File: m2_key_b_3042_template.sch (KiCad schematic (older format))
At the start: 1 part, among them J1 M.2_Key_B

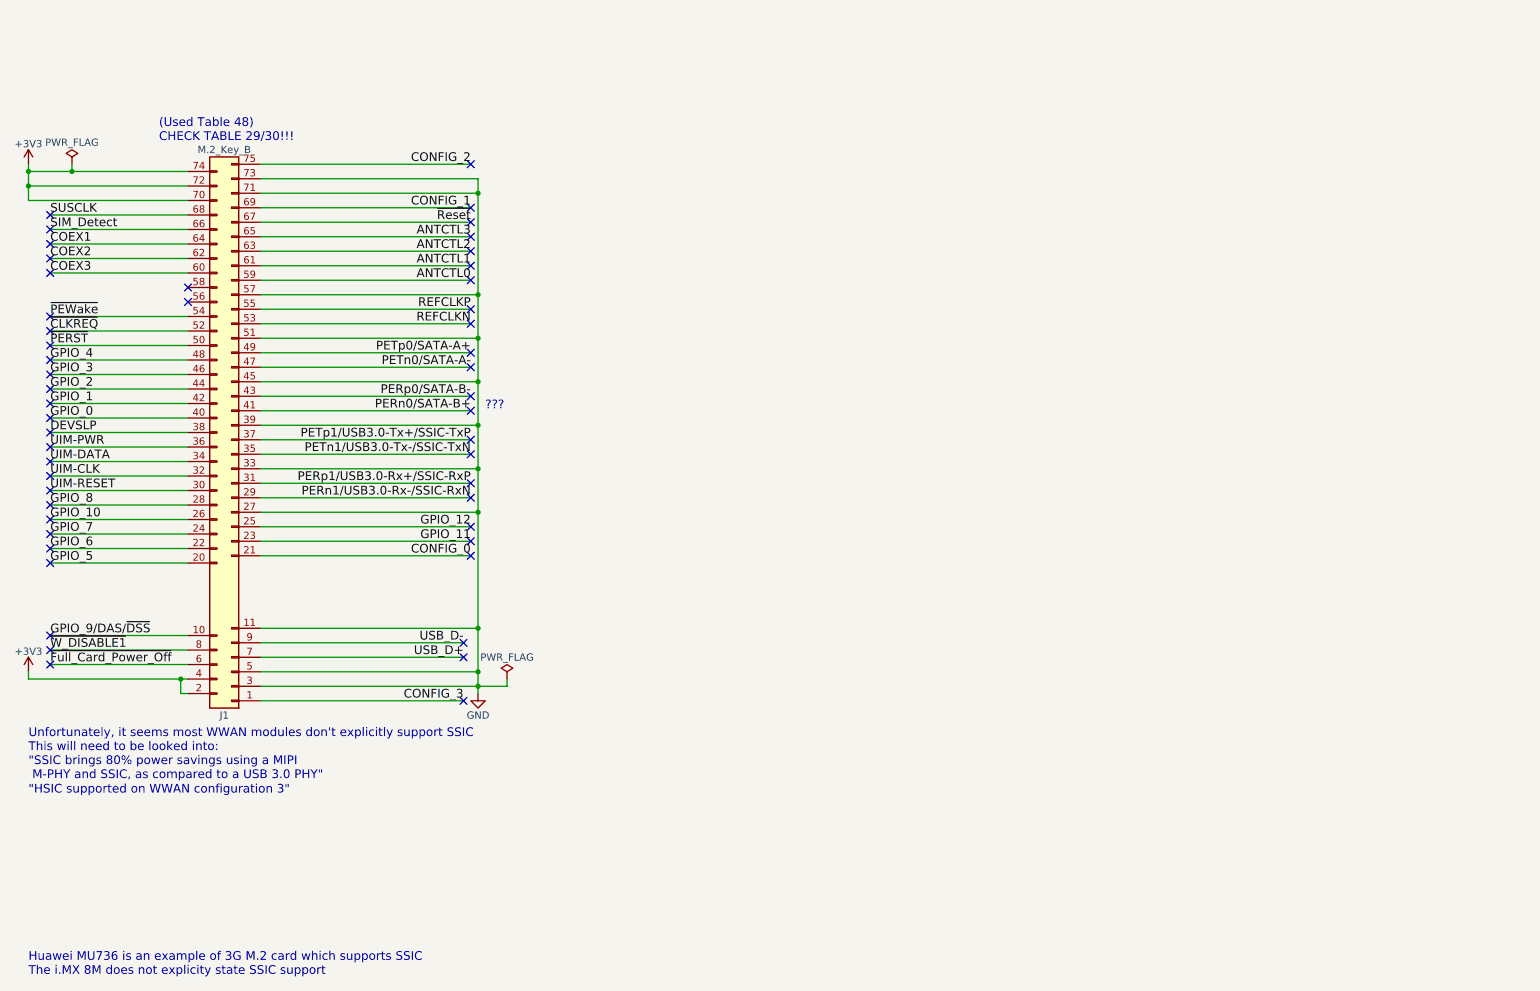
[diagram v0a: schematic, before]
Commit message: Include MHF4 coax connectors for the baseband, diversity, and GNSS antennae
Improved the soldermask and mounting hole.
Included silkscreen designating the component area.
Antennae MHF4 coax connectors show what orientation they need to be placed in (chamfer).
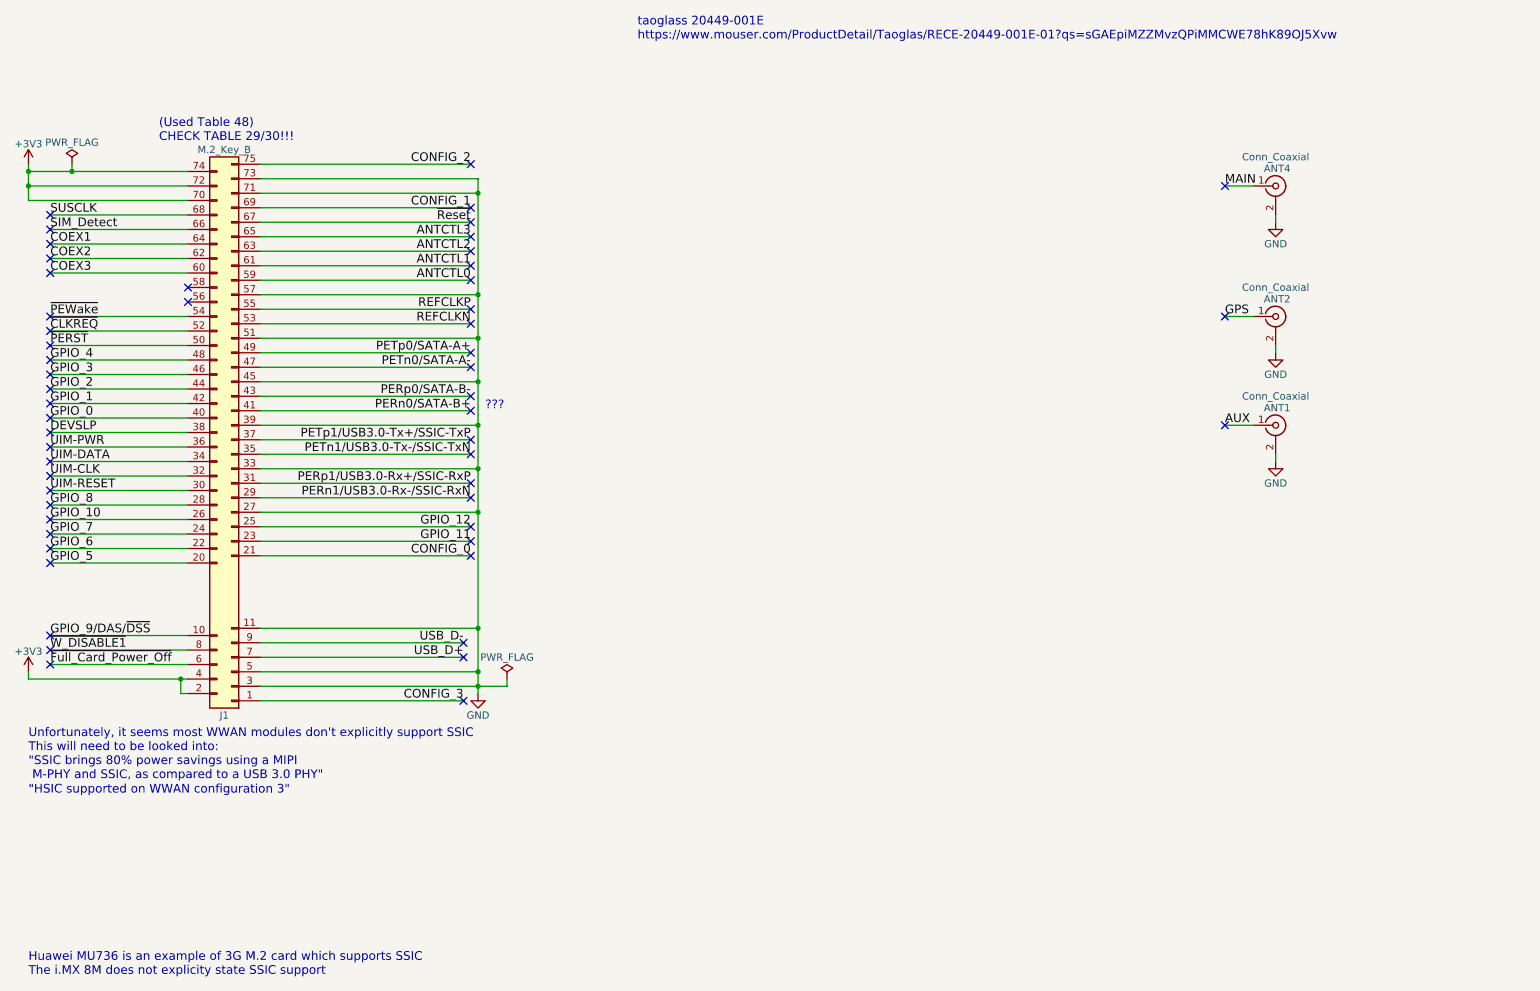
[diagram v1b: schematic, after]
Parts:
- added ANT1, ANT2, ANT4: Conn_Coaxial, m2_key_b_3042:MHF4_20449-001E, symbol Conn_Coaxial
- J1: footprint m2_key_b:m2_key_b_gold_fingers -> m2_key_b_3042:M.2_Key_B_Gold_Fingers
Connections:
- net GND: now also ANT1.2 (Ext), ANT2.2 (Ext), ANT4.2 (Ext)
- new net AUX: ANT1.1 (In)
- new net GPS: ANT2.1 (In)
- new net MAIN: ANT4.1 (In)
- no-connect marks 51 -> 54
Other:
- note added: "taoglass 20449-001E\nhttps://www.mouser.com/ProductDetail/Taoglas/RECE-20449-001E-01?qs=sGAEpiMZZMvzQPiMMCWE78hK89OJ5Xvw"
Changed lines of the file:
@@
 LIBS:contrib
 LIBS:valves
-LIBS:m2_key_b_template
-LIBS:m2_key_b_template-cache
+LIBS:m2_key_b_3042_template
+LIBS:m2_key_b_3042_template-cache
 EELAYER 25 0
 EELAYER END
@@
 F 0 "J1" H 3000 5600 50  0000 C CNN
 F 1 "M.2_Key_B" H 3000 1700 50  0000 C CNN
-F 2 "m2_key_b:m2_key_b_gold_fingers" H 2950 3700 50  0001 C CNN
+F 2 "m2_key_b_3042:M.2_Key_B_Gold_Fingers" H 2950 3700 50  0001 C CNN
 F 3 "" H 2950 3700 50  0001 C CNN
 	1    2950 3700
@@
 $EndComp
 Wire Wire Line
-	2650 1850 1550 1850
+	1550 1850 2650 1850
 Wire Wire Line
 	1550 1800 1550 2050
@@
 Wire Wire Line
 	4850 5400 4850 5350
+Text Notes 5750 950  0    60   ~ 0
+taoglass 20449-001E\nhttps://www.mouser.com/ProductDetail/Taoglas/RECE-20449-001E-01?qs=sGAEpiMZZMvzQPiMMCWE78hK89OJ5Xvw
+$Comp
+L Conn_Coaxial ANT1
+U 1 1 5AA9D3C4
+P 10150 3600
+F 0 "ANT1" H 10160 3720 50  0000 C CNN
+F 1 "Conn_Coaxial" H 10150 3800 50  0000 C CNN
+F 2 "m2_key_b_3042:MHF4_20449-001E" H 10150 3600 50  0001 C CNN
+F 3 "" H 10150 3600 50  0001 C CNN
+	1    10150 3600
+	1    0    0    -1
+$EndComp
+$Comp
+L Conn_Coaxial ANT2
+U 1 1 5AA9D4DD
+P 10150 2850
+F 0 "ANT2" H 10160 2970 50  0000 C CNN
+F 1 "Conn_Coaxial" H 10150 3050 50  0000 C CNN
+F 2 "m2_key_b_3042:MHF4_20449-001E" H 10150 2850 50  0001 C CNN
+F 3 "" H 10150 2850 50  0001 C CNN
+	1    10150 2850
+	1    0    0    -1
+$EndComp
+$Comp
+L Conn_Coaxial ANT4
+U 1 1 5AA9D54E
+P 10150 1950
+F 0 "ANT4" H 10160 2070 50  0000 C CNN
+F 1 "Conn_Coaxial" H 10150 2150 50  0000 C CNN
+F 2 "m2_key_b_3042:MHF4_20449-001E" H 10150 1950 50  0001 C CNN
+F 3 "" H 10150 1950 50  0001 C CNN
+	1    10150 1950
+	1    0    0    -1
+$EndComp
+$Comp
+L GND #PWR06
+U 1 1 5AA9D64F
+P 10150 2200
+F 0 "#PWR06" H 10150 1950 50  0001 C CNN
+F 1 "GND" H 10150 2050 50  0000 C CNN
+F 2 "" H 10150 2200 50  0001 C CNN
+F 3 "" H 10150 2200 50  0001 C CNN
+	1    10150 2200
+	1    0    0    -1
+$EndComp
+$Comp
+L GND #PWR07
+U 1 1 5AA9D6ED
+P 10150 3100
+F 0 "#PWR07" H 10150 2850 50  0001 C CNN
+F 1 "GND" H 10150 2950 50  0000 C CNN
+F 2 "" H 10150 3100 50  0001 C CNN
+F 3 "" H 10150 3100 50  0001 C CNN
+	1    10150 3100
+	1    0    0    -1
+$EndComp
+$Comp
+L GND #PWR08
+U 1 1 5AA9D704
+P 10150 3850
+F 0 "#PWR08" H 10150 3600 50  0001 C CNN
+F 1 "GND" H 10150 3700 50  0000 C CNN
+F 2 "" H 10150 3850 50  0001 C CNN
+F 3 "" H 10150 3850 50  0001 C CNN
+	1    10150 3850
+	1    0    0    -1
+$EndComp
+Wire Wire Line
+	10150 3100 10150 3050
+Wire Wire Line
+	10150 2200 10150 2150
+Wire Wire Line
+	10150 3850 10150 3800
+Wire Wire Line
+	10000 3600 9800 3600
+Wire Wire Line
+	10000 2850 9800 2850
+Wire Wire Line
+	10000 1950 9800 1950
+Text Label 9800 3600 0    60   ~ 0
+AUX
+Text Label 9800 2850 0    60   ~ 0
+GPS
+Text Label 9800 1950 0    60   ~ 0
+MAIN
+NoConn ~ 9800 3600
+NoConn ~ 9800 2850
+NoConn ~ 9800 1950
 $EndSCHEMATC
